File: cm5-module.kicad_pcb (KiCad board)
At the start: 4 copper layers, 100 x 100 mm, 244 parts, among them J1 DIN-41612-connector_090319679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, J10 MicroSD_5033981892, J11 JST_SH_1x4_BM04B-SRSS-TB-LF-SN, J13 USB-C_TYPE-C_16PLT-H6.5, J2 CM5_1-100_3mm-stack, J3 CM5_101-200_3mm-stack, J4 JST_SH_1x3_BM03B-SRSS-TB-LF-SN, J5 Bus_M.2_1-2199230-6, J6 RJ45_HC612601A-M893-A, J7 USB-A_USB-303WSD-BRY, J8 HDMI-A_HDMI-19PIN-043, J9 USB-C_USB-310F-B-SU, Q1 SIS472DN-T1-GE3, Q10 AO3400A, Q2 SIS472DN-T1-GE3, Q3 AO3400A, Q4 SIS472DN-T1-GE3, Q5 AO3400A, Q6 AO3400A, Q7 AO3400A, Q8 AO3401A, Q9 AO3401A, SW1 SW_TL2243, U1 AP22615AWU-7, U10 AP22615AWU-7, U11 AP22615AWU-7, U12 LM74700QDBVRQ1, U13 STM32G431CBU6, U14 STM32G431CBU6, U15 TJA1044GTK_3Z, U16 TJA1044GTK_3Z, U17 FSUSB42UMX, U2 AP22615AWU-7, U3 FT230XQ-R, U4 NTS0102DP, U5 CH334P, U6 LM74700QDBVRQ1, U7 SIC431AED-T1-GE3, U8 LM74700QDBVRQ1, U9 TPS564247DRLR, Y1 Oscillator_32.768kHz_OK2EL89C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, Y2 X322512MSB4SI

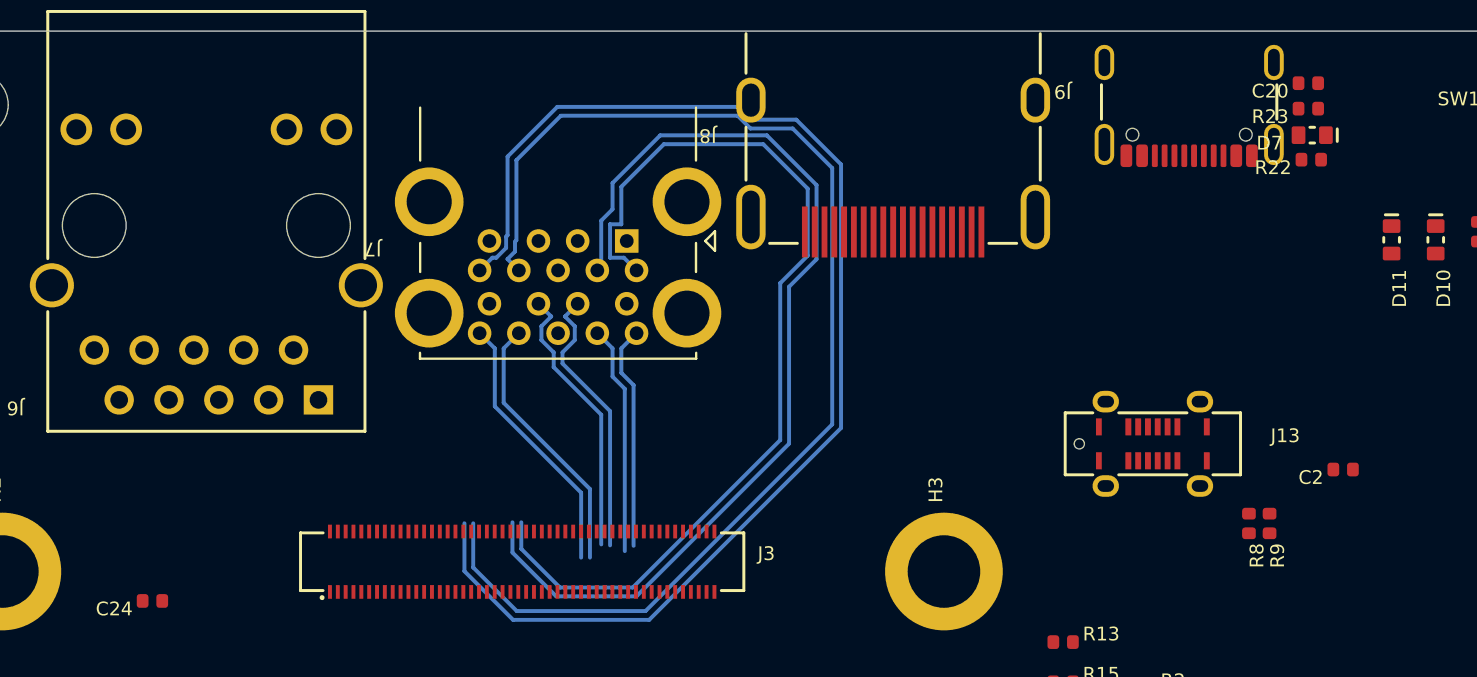
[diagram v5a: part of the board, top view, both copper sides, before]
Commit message: [#3] Add TVS, route HDMI and fanout ETH
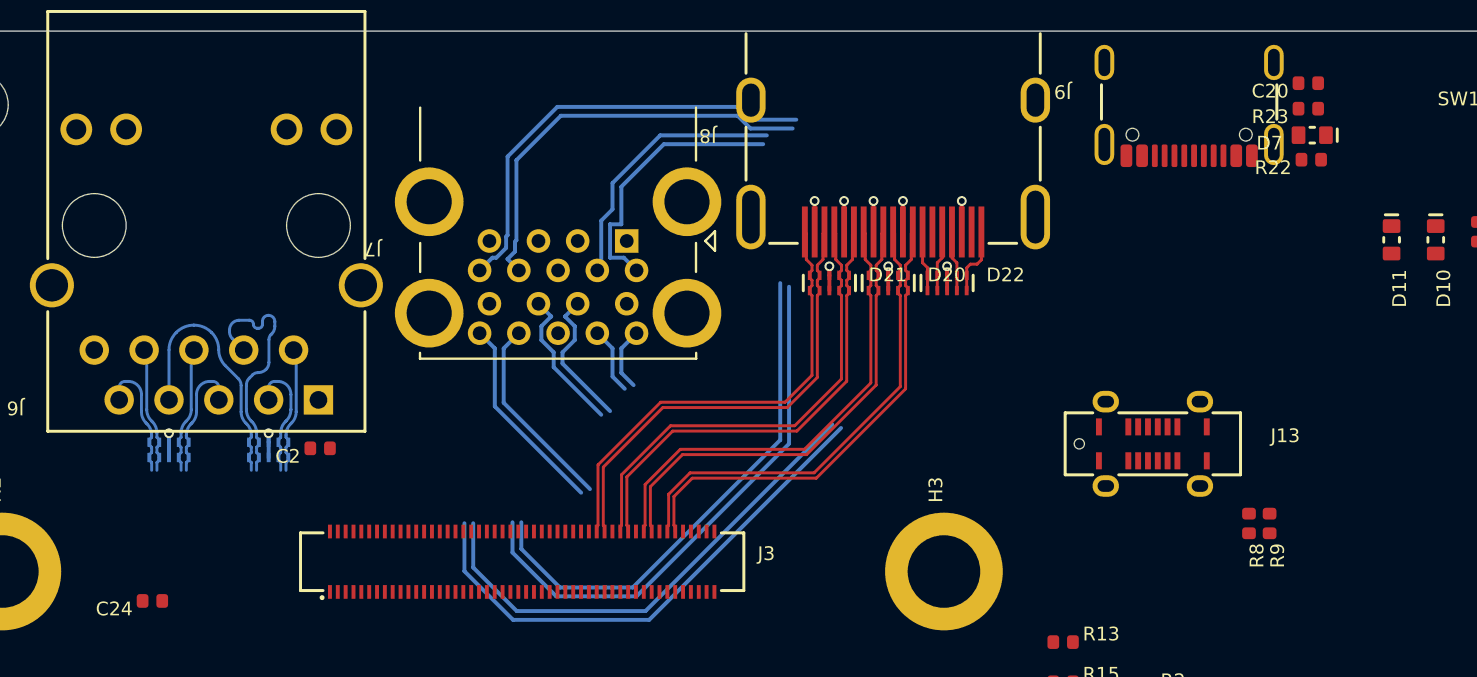
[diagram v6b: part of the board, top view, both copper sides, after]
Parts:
- added D17: PUSB3F96X, DW-footprints:SOT1176-1, B.Cu at (61.1, 71.3)
- added D19: PUSB3F96X, DW-footprints:SOT1176-1, B.Cu at (56.0, 71.3)
- added D20: PUSB3F96X, DW-footprints:SOT1176-1, F.Cu at (92.7, 62.8)
- added D21: PUSB3F96X, DW-footprints:SOT1176-1, F.Cu at (89.7, 62.8)
- added D22: PUSB3F96X, DW-footprints:SOT1176-1, F.Cu at (95.7, 62.8)
- moved C2 52.2 mm to (63.8, 71.3)
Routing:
- net /CM5/HDMI_0.CLK+: track 0.00 -> 24.2 mm
- net /CM5/HDMI_0.CLK-: track 0.00 -> 24.2 mm
- net /CM5/HDMI_0.D0+: track 0.00 -> 24.1 mm
- net /CM5/HDMI_0.D0-: track 0.00 -> 24.1 mm
- net /CM5/HDMI_0.D1+: track 0.00 -> 24.0 mm
- net /CM5/HDMI_0.D1-: track 0.00 -> 24.0 mm
- net /CM5/HDMI_0.D2+: track 0.00 -> 23.9 mm
- net /CM5/HDMI_0.D2-: track 0.00 -> 23.9 mm
- net /CM5/USB_SS_0.RX-: track 65.9 -> 49.3 mm
- net /CM5/USB_SS_0.RX+: track 62.7 -> 46.8 mm
- net GND: track 20.4 -> 34.5 mm, vias 29 -> 39
- net /CM5/ETH.D2-: track 0.00 -> 13.4 mm
- net /CM5/ETH.D2+: track 0.00 -> 13.3 mm
- net /CM5/USB_SS_0.TX-: track 50.9 -> 41.5 mm
- net /CM5/USB_SS_0.TX+: track 49.0 -> 40.4 mm
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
